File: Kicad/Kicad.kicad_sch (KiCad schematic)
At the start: 0 parts

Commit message: power section
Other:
- sheet DSP ports: added USB1_DM, USB1_DP, USB1_VBUS, USB1_VDD3V3; removed none
- sheet USB ports: added USB0_DM_CON, USB0_DP_CON, USB0_VBUS_CON; removed none
- note removed: "3v3"
- note removed: "5V"
- note removed: "ADC"
- note removed: "Analog in"
- note removed: "Analog out"
- note removed: "Buck"
- note removed: "DAC"
- note removed: "DSP"
- note removed: "Digital out"
- note removed: "Flash"
- note removed: "LDO"
- note removed: "MCU"
- note removed: "SPDIF connector"
- note removed: "SWITCH"
- note removed: "USB Connector"
- note removed: "USB-Audio"
- note removed: "VBUS"
- note removed: "VSUP"
- note removed: "i2S in"
- note removed: "i2S out"

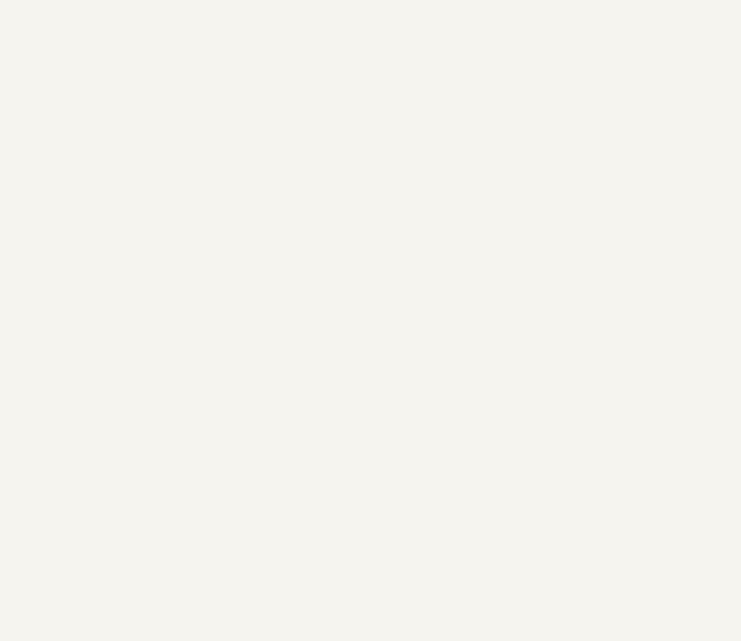
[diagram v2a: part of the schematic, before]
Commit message: moved Buck to external components sheet
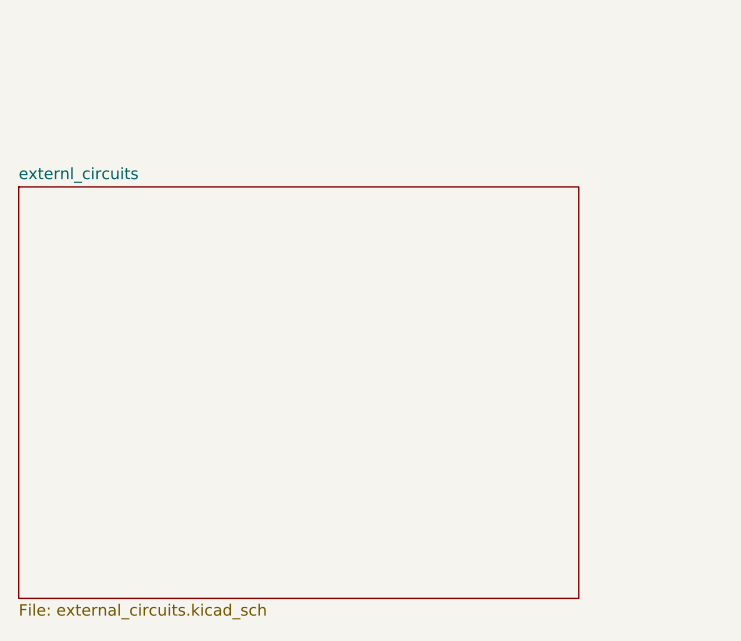
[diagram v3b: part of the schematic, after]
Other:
- added sheet externl_circuits (external_circuits.kicad_sch)
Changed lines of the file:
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@@
+    )
+  )
+  (sheet (at 24.13 143.51) (size 62.23 45.72) (fields_autoplaced)
+    (stroke (width 0.1524) (type solid) (color 0 0 0 0))
+    (fill (color 0 0 0 0.0000))
+    (property "Sheet name" "externl_circuits" (id 0) (at 24.13 142.7984 0)
+      (effects (font (size 1.27 1.27)) (justify left bottom))
+    )
+    (property "Sheet file" "external_circuits.kicad_sch" (id 1) (at 24.13 189.8146 0)
+      (effects (font (size 1.27 1.27)) (justify left top))
     )
   )
@@
     (path "/0502a4b7-f1e4-41d1-b3cb-3e756a9c03ee" (page "4"))
     (path "/fc70b7b5-40ea-48ba-b37b-91c92dde031f" (page "5"))
+    (path "/f57a1676-bccf-420e-8992-39ff2da9b98b" (page "6"))
   )
   (symbol_instances
@@
       (reference "#PWR08") (unit 1) (value "GND") (footprint "")
     )
-    (path "/fc70b7b5-40ea-48ba-b37b-91c92dde031f/5e6df6f5-7f96-434e-831c-ec55b1a48c51"
-      (reference "#PWR09") (unit 1) (value "GND") (footprint "")
-    )
     (path "/fc70b7b5-40ea-48ba-b37b-91c92dde031f/f57de093-c5a7-454f-9b27-98057cee1693"
       (reference "#PWR010") (unit 1) (value "GND") (footprint "")
-    )
-    (path "/fc70b7b5-40ea-48ba-b37b-91c92dde031f/c1d99d8d-b5cd-43b7-8e40-092891ddb5e0"
-      (reference "#PWR011") (unit 1) (value "GND") (footprint "")
     )
     (path "/fc70b7b5-40ea-48ba-b37b-91c92dde031f/ca0f76e4-dc2f-4499-85e5-b1770c28458f"
       (reference "#PWR012") (unit 1) (value "GND") (footprint "")
     )
-    (path "/fc70b7b5-40ea-48ba-b37b-91c92dde031f/e2a8d705-e2bd-4baa-b7a3-266125006d15"
-      (reference "#PWR013") (unit 1) (value "GND") (footprint "")
-    )
-    (path "/fc70b7b5-40ea-48ba-b37b-91c92dde031f/c39b1adc-edc1-4586-bd8b-77d35e9c61e0"
-      (reference "#PWR014") (unit 1) (value "GND") (footprint "")
-    )
-    (path "/fc70b7b5-40ea-48ba-b37b-91c92dde031f/bc835362-7dda-427e-9fc6-43970fc16828"
-      (reference "#PWR015") (unit 1) (value "GND") (footprint "")
-    )
     (path "/fc70b7b5-40ea-48ba-b37b-91c92dde031f/a77cfac3-6742-458a-aa29-b17d11f301d9"
       (reference "#PWR016") (unit 1) (value "GND") (footprint "")
+    )
+    (path "/f57a1676-bccf-420e-8992-39ff2da9b98b/0634a78b-175c-4996-b962-42c146622575"
+      (reference "#PWR?") (unit 1) (value "GND") (footprint "")
+    )
+    (path "/f57a1676-bccf-420e-8992-39ff2da9b98b/42b5ada7-c631-46de-b36f-8560977928b8"
+      (reference "#PWR?") (unit 1) (value "GND") (footprint "")
+    )
+    (path "/f57a1676-bccf-420e-8992-39ff2da9b98b/8d127f63-d07c-4b77-b633-f7bb7dd0023d"
+      (reference "#PWR?") (unit 1) (value "GND") (footprint "")
+    )
+    (path "/f57a1676-bccf-420e-8992-39ff2da9b98b/b166d854-f865-4e61-9bba-e340da732546"
+      (reference "#PWR?") (unit 1) (value "GND") (footprint "")
+    )
+    (path "/f57a1676-bccf-420e-8992-39ff2da9b98b/c64ba410-493d-451f-a90d-7a5e267c4eba"
+      (reference "#PWR?") (unit 1) (value "GND") (footprint "")
     )
     (path "/14104a26-f0d1-4bb5-95a4-061659058c78/d190749c-3b3f-48f0-a118-658c9db977cd"
       (reference "C1") (unit 1) (value "2u2") (footprint "Capacitor_SMD:C_0805_2012Metric")
     )
-    (path "/fc70b7b5-40ea-48ba-b37b-91c92dde031f/8f1c4c2c-960c-4841-874d-5bcfec261a5f"
-      (reference "C2") (unit 1) (value "4u7") (footprint "Capacitor_SMD:C_0805_2012Metric")
-    )
     (path "/fc70b7b5-40ea-48ba-b37b-91c92dde031f/780efb4b-ea77-4516-b22b-3597dc85d413"
       (reference "C3") (unit 1) (value "1u") (footprint "Capacitor_SMD:C_0805_2012Metric")
     )
-    (path "/fc70b7b5-40ea-48ba-b37b-91c92dde031f/28d32f31-3dcf-4a1a-8ae6-8a05d5724ca9"
-      (reference "C4") (unit 1) (value "4u7") (footprint "Capacitor_SMD:C_0805_2012Metric")
-    )
     (path "/fc70b7b5-40ea-48ba-b37b-91c92dde031f/f22b33bb-5f1f-4f01-97b0-d58af0631724"
       (reference "C5") (unit 1) (value "1u") (footprint "Capacitor_SMD:C_0805_2012Metric")
-    )
-    (path "/fc70b7b5-40ea-48ba-b37b-91c92dde031f/06cf598c-18ee-4964-adf6-333364947093"
-      (reference "C6") (unit 1) (value "100uF") (footprint "Capacitor_THT:CP_Radial_D10.0mm_P5.00mm")
-    )
-    (path "/fc70b7b5-40ea-48ba-b37b-91c92dde031f/6cbfdfaf-cf10-4f9d-9691-f685b7efc29b"
-      (reference "C7") (unit 1) (value "1u") (footprint "Capacitor_SMD:C_0805_2012Metric")
-    )
-    (path "/fc70b7b5-40ea-48ba-b37b-91c92dde031f/970db952-49f9-49a7-a34d-be9c07a302df"
-      (reference "C8") (unit 1) (value "100uF") (footprint "Capacitor_THT:CP_Radial_D10.0mm_P5.00mm")
-    )
-    (path "/fc70b7b5-40ea-48ba-b37b-91c92dde031f/877e627a-5915-4f32-b224-b5864023ca7a"
-      (reference "C9") (unit 1) (value "1u") (footprint "Capacitor_SMD:C_0805_2012Metric")
     )
     (path "/fc70b7b5-40ea-48ba-b37b-91c92dde031f/1f171868-fac2-4e0d-9075-5f6cd6da7010"
@@
       (reference "C11") (unit 1) (value "10uF") (footprint "Capacitor_SMD:C_0805_2012Metric")
     )
-    (path "/fc70b7b5-40ea-48ba-b37b-91c92dde031f/23c2a8be-3964-40da-8713-936e89d30ee2"
-      (reference "CIN1") (unit 1) (value "0.022uF") (footprint "Capacitor_SMD:C_1206_3216Metric")
+    (path "/f57a1676-bccf-420e-8992-39ff2da9b98b/2ce8521d-b4f6-41fe-a3f6-e943f0a06d49"
+      (reference "C?") (unit 1) (value "100uF") (footprint "Capacitor_THT:CP_Radial_D10.0mm_P5.00mm")
     )
-    (path "/fc70b7b5-40ea-48ba-b37b-91c92dde031f/7d9f41a9-c3db-4f89-8268-a8ae69e6a661"
-      (reference "CIN2") (unit 1) (value "0.022uF") (footprint "Capacitor_SMD:C_1206_3216Metric")
+    (path "/f57a1676-bccf-420e-8992-39ff2da9b98b/315b4fca-3370-4854-a18f-e38da14b8fa2"
+      (reference "C?") (unit 1) (value "4u7") (footprint "Capacitor_SMD:C_0805_2012Metric")
     )
-    (path "/fc70b7b5-40ea-48ba-b37b-91c92dde031f/0b762d42-3c26-4c09-97b6-3462e5400f48"
-      (reference "CONN1") (unit 1) (value "Screw_Terminal_01x02") (footprint "TerminalBlock_Phoenix:TerminalBlock_Phoenix_MKDS-1,5-2_1x02_P5.00mm_Horizontal")
+    (path "/f57a1676-bccf-420e-8992-39ff2da9b98b/5b8359f8-700c-4aba-8a17-3ae0fdd76efc"
+      (reference "C?") (unit 1) (value "1u") (footprint "Capacitor_SMD:C_0805_2012Metric")
+    )
+    (path "/f57a1676-bccf-420e-8992-39ff2da9b98b/7b2e5c6d-6629-4392-ab6b-b87d7d5b3b79"
+      (reference "C?") (unit 1) (value "1u") (footprint "Capacitor_SMD:C_0805_2012Metric")
+    )
+    (path "/f57a1676-bccf-420e-8992-39ff2da9b98b/8b14ef2e-12af-4862-b44e-89f80b6b7488"
+      (reference "C?") (unit 1) (value "100uF") (footprint "Capacitor_THT:CP_Radial_D10.0mm_P5.00mm")
+    )
+    (path "/f57a1676-bccf-420e-8992-39ff2da9b98b/b1fc679d-2c6d-438e-b63d-352c9517b3a1"
+      (reference "C?") (unit 1) (value "4u7") (footprint "Capacitor_SMD:C_0805_2012Metric")
+    )
+    (path "/f57a1676-bccf-420e-8992-39ff2da9b98b/1b6a5ba2-ca0d-48e9-bdec-3b9998d5d68a"
+      (reference "CIN?") (unit 1) (value "0.022uF") (footprint "Capacitor_SMD:C_1206_3216Metric")
+    )
+    (path "/f57a1676-bccf-420e-8992-39ff2da9b98b/38bce711-2385-413d-a92e-b71c3f144ec4"
+      (reference "CIN?") (unit 1) (value "0.022uF") (footprint "Capacitor_SMD:C_1206_3216Metric")
+    )
+    (path "/f57a1676-bccf-420e-8992-39ff2da9b98b/1bae38ac-be07-4072-b319-f42a478f8a83"
+      (reference "CONN?") (unit 1) (value "Screw_Terminal_01x02") (footprint "TerminalBlock_Phoenix:TerminalBlock_Phoenix_MKDS-1,5-2_1x02_P5.00mm_Horizontal")
     )
     (path "/14104a26-f0d1-4bb5-95a4-061659058c78/f19920a9-adcd-4f8a-852d-0752a7080bd1"
@@
       (reference "L1") (unit 1) (value "330") (footprint "Inductor_SMD:L_1210_3225Metric")
     )
-    (path "/fc70b7b5-40ea-48ba-b37b-91c92dde031f/3ae8ce1e-2211-4417-a2b1-1b1b7a211456"
-      (reference "L2") (unit 1) (value "47") (footprint "Inductor_SMD:L_2010_5025Metric")
+    (path "/f57a1676-bccf-420e-8992-39ff2da9b98b/721bb39b-5084-4007-9fcb-81952d384cfd"
+      (reference "L?") (unit 1) (value "47") (footprint "Inductor_SMD:L_2010_5025Metric")
     )
-    (path "/fc70b7b5-40ea-48ba-b37b-91c92dde031f/49aaa3ac-6131-4eb2-b800-68e55838b888"
-      (reference "L3") (unit 1) (value "4u7") (footprint "Inductor_SMD:L_2010_5025Metric")
-    )
-    (path "/fc70b7b5-40ea-48ba-b37b-91c92dde031f/3292f810-6daa-4d9e-923e-ae09c6deef70"
-      (reference "R1") (unit 1) (value "0.1R") (footprint "Resistor_SMD:R_2512_6332Metric")
-    )
-    (path "/fc70b7b5-40ea-48ba-b37b-91c92dde031f/4369ed3e-bd0d-4623-b109-f2e287dd42e5"
-      (reference "R2") (unit 1) (value "20k") (footprint "Resistor_SMD:R_0805_2012Metric")
+    (path "/f57a1676-bccf-420e-8992-39ff2da9b98b/f397aadd-05ce-4cf7-beb1-d83d38f41a4b"
+      (reference "L?") (unit 1) (value "4u7") (footprint "Inductor_SMD:L_2010_5025Metric")
     )
     (path "/fc70b7b5-40ea-48ba-b37b-91c92dde031f/8d07fdbf-02bf-4cea-9bfc-4dfb29a273ce"
       (reference "R3") (unit 1) (value "10k") (footprint "Resistor_SMD:R_0805_2012Metric")
+    )
+    (path "/f57a1676-bccf-420e-8992-39ff2da9b98b/0e27d7a6-7465-466f-ba93-ae7d8297a197"
+      (reference "R?") (unit 1) (value "0.1R") (footprint "Resistor_SMD:R_2512_6332Metric")
+    )
+    (path "/f57a1676-bccf-420e-8992-39ff2da9b98b/2a57f5d7-a323-407b-bea4-1b5f2ab78b93"
+      (reference "R?") (unit 1) (value "20k") (footprint "Resistor_SMD:R_0805_2012Metric")
     )
     (path "/6df5daab-4c21-4240-9816-377e45d59fb9/d03b6aeb-93cb-43e1-b6e8-27690f2c8d1a"
@@
       (reference "U1") (unit 4) (value "MIMXRT685SFVKB") (footprint "project_footprints:BGA-289_17x17_9.0x9.0mm_v2")
     )
-    (path "/fc70b7b5-40ea-48ba-b37b-91c92dde031f/eaec849c-2851-496e-881c-35a173c2a609"
-      (reference "U2") (unit 1) (value "MAX16903RAUE50/V+") (footprint "project_footprints:MAX16903RAUE50&slash_V&plus_")
-    )
     (path "/fc70b7b5-40ea-48ba-b37b-91c92dde031f/af971651-05f3-44cd-9341-b1a9ba290600"
       (reference "U3") (unit 1) (value "TPS76718QD") (footprint "project_footprints:TPS76718QD")
     )
+    (path "/f57a1676-bccf-420e-8992-39ff2da9b98b/130a151c-5a9e-4acd-9331-4d5a112b395f"
+      (reference "U?") (unit 1) (value "MAX16903RAUE50/V+") (footprint "project_footprints:MAX16903RAUE50&slash_V&plus_")
+    )
     (path "/6df5daab-4c21-4240-9816-377e45d59fb9/99292b52-1e32-45b0-8600-21b94125ccf4"

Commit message: working on DSP
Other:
- added sheet DAC (DAC.kicad_sch)

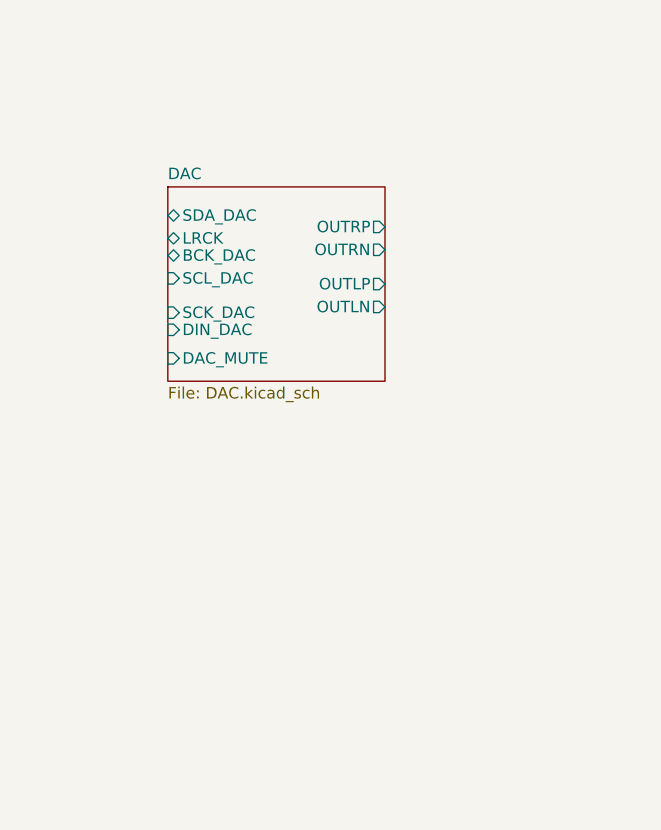
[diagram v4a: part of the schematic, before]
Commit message: changed dac to ES9033
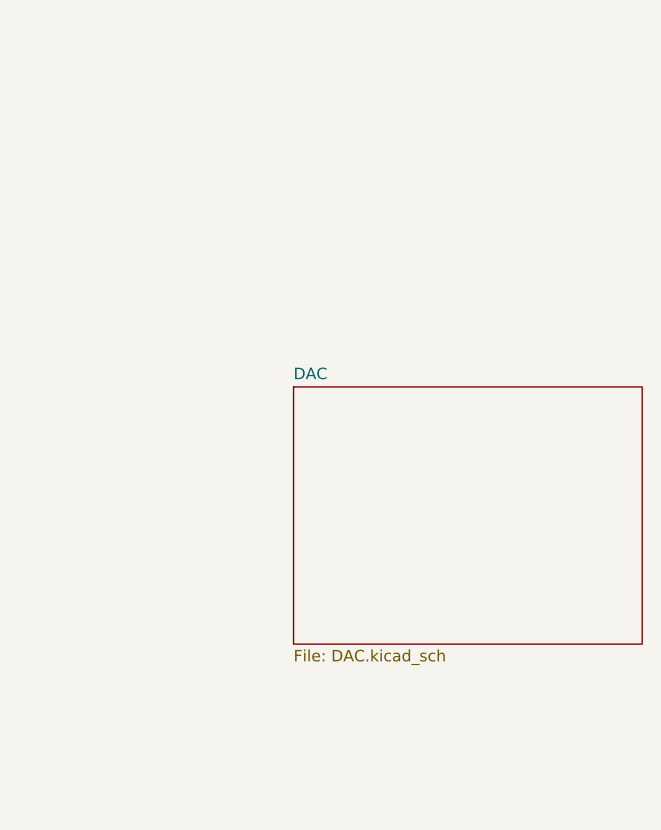
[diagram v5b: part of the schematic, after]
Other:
- sheet DAC ports: added none; removed BCK_DAC, DAC_MUTE, DIN_DAC, LRCK, OUTLN, OUTLP, OUTRN, OUTRP, SCK_DAC, SCL_DAC, SDA_DAC

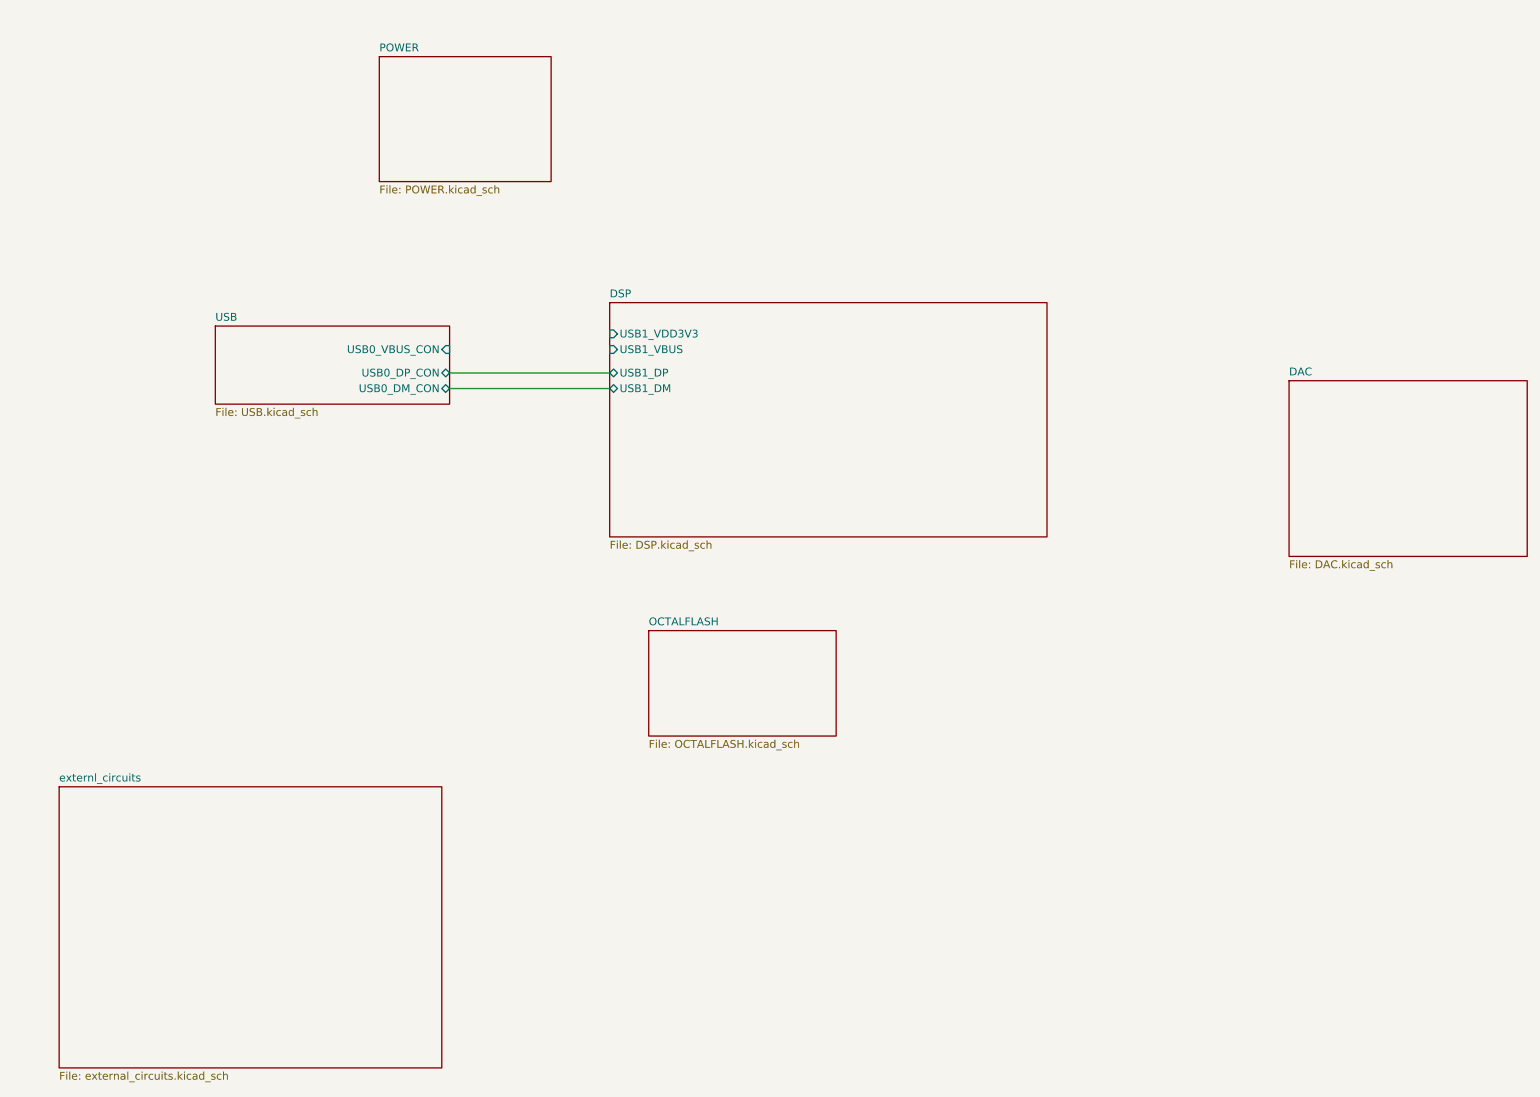
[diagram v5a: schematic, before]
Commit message: updated DAC circut
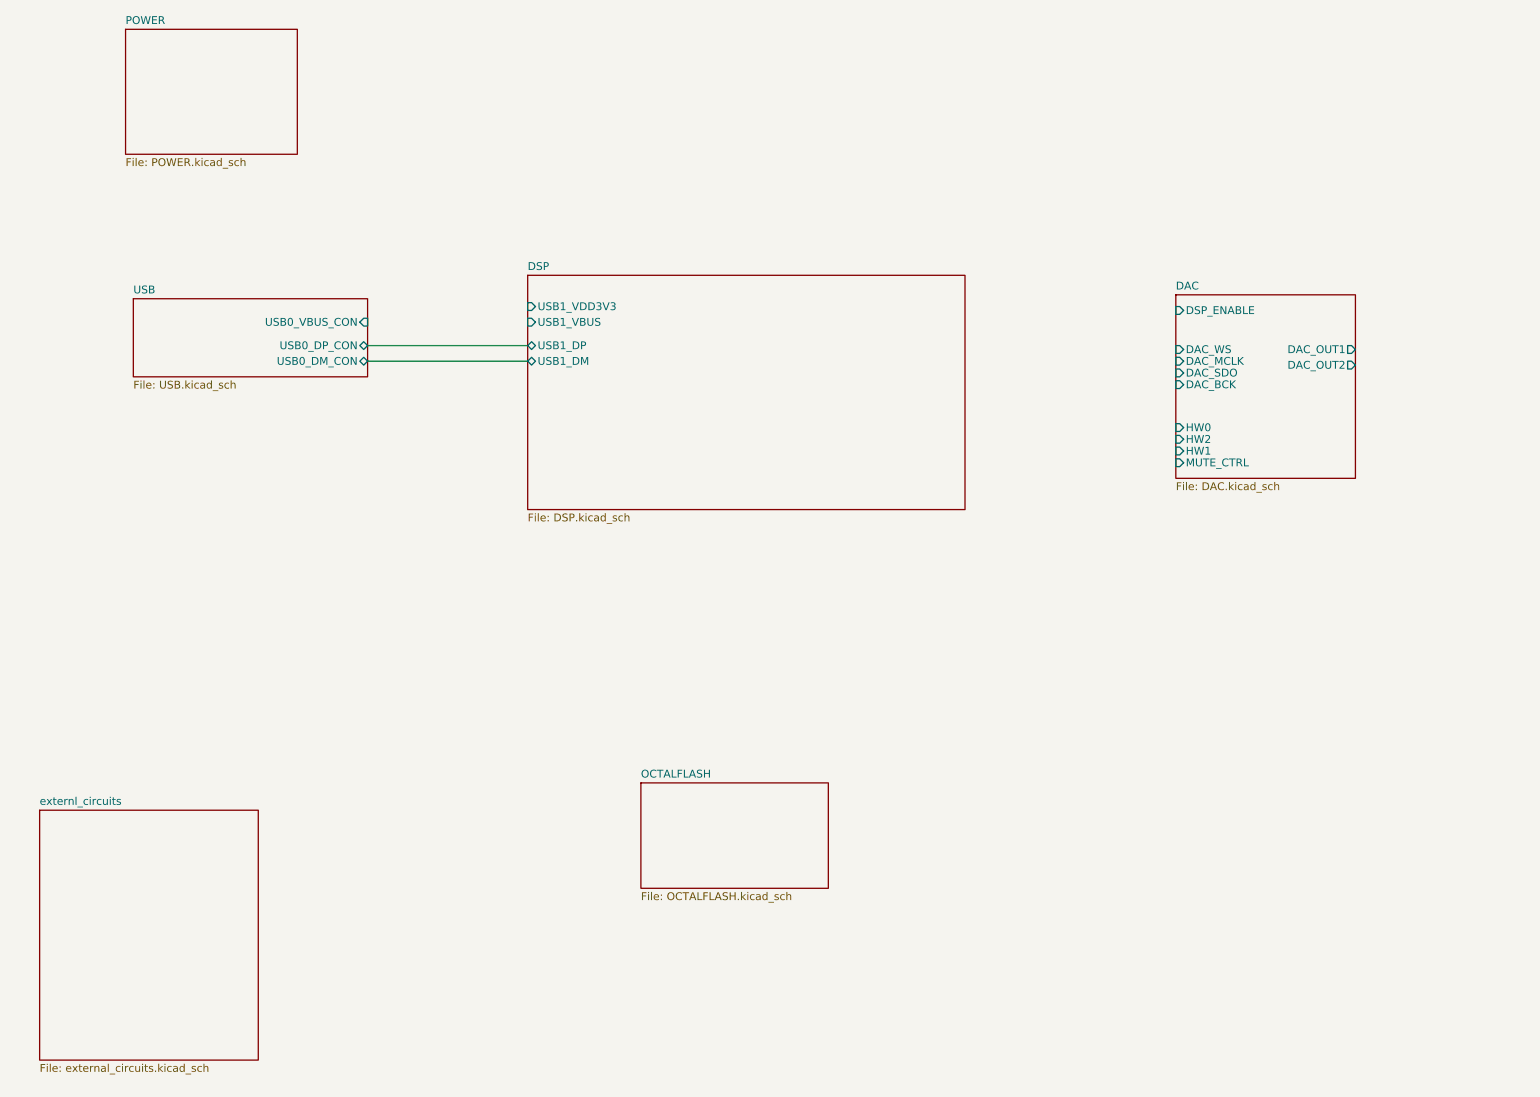
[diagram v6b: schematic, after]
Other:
- sheet DAC ports: added DAC_BCK, DAC_MCLK, DAC_OUT1, DAC_OUT2, DAC_SDO, DAC_WS, DSP_ENABLE, HW0, HW1, HW2, MUTE_CTRL; removed none
